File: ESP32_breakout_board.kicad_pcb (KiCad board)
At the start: 2 copper layers, 55.2 x 55.9 mm, 12 parts, among them J1 Conn_01x15, J2 Conn_01x15

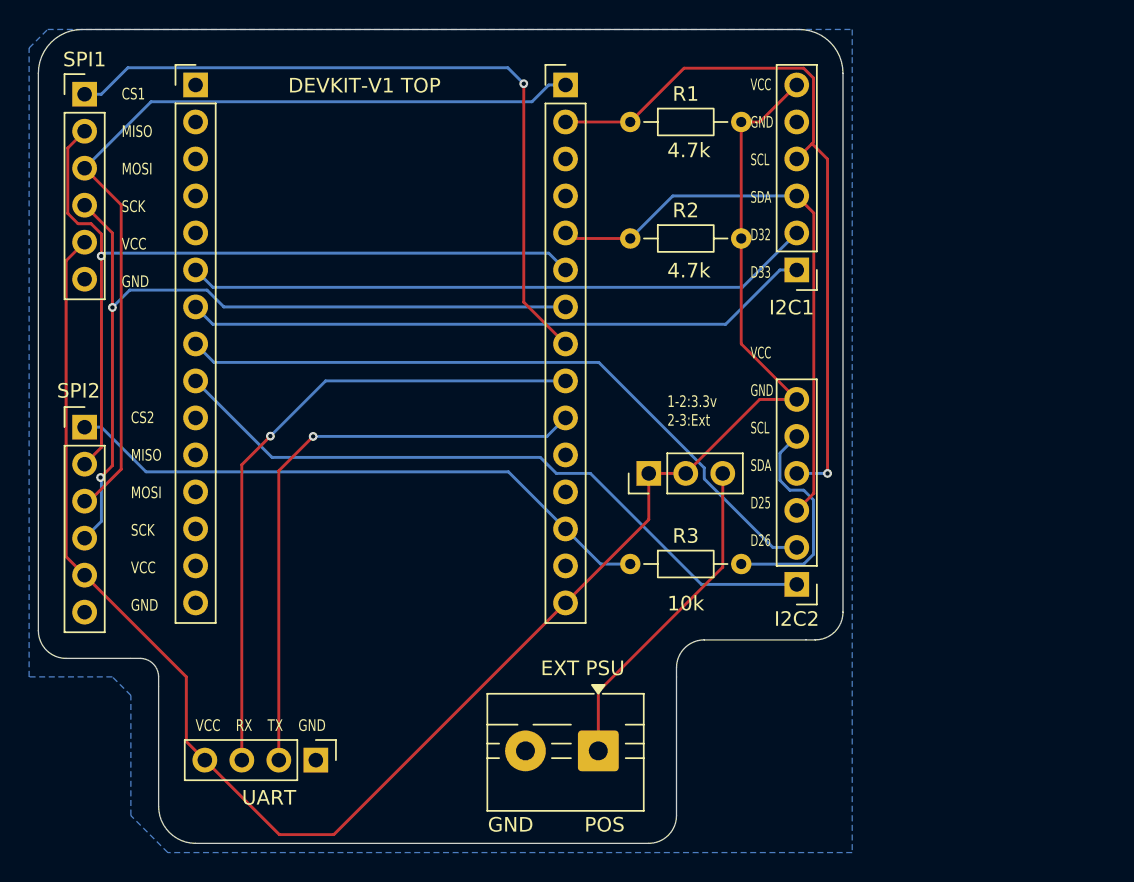
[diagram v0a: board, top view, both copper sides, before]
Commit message: changed design
removed the 10k pull down after careful consideration and cleaned up the design a bit
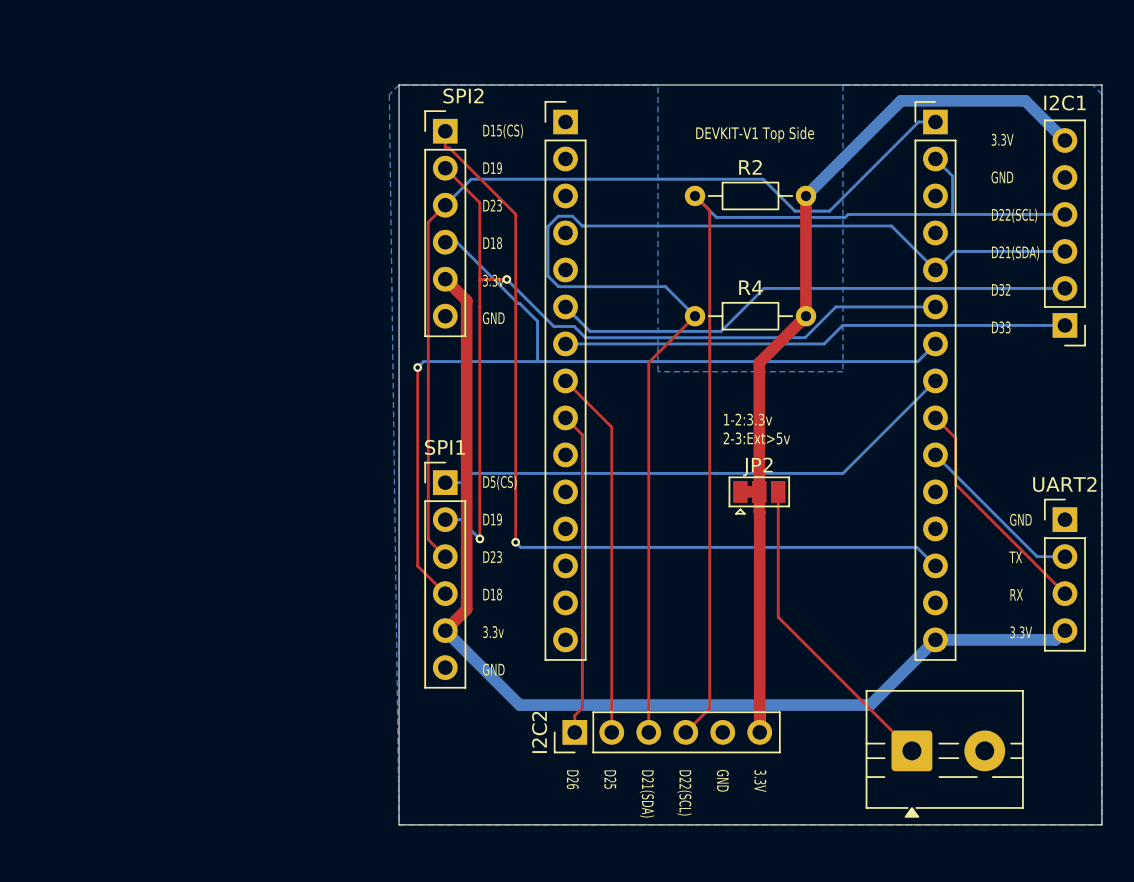
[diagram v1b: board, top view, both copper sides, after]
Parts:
- removed JP1: Power select jumper, Connector_PinHeader_2.54mm:PinHeader_1x03_P2.54mm_Vertical
- removed R1: 4.7k, Resistor_THT:R_Axial_DIN0204_L3.6mm_D1.6mm_P7.62mm_Horizontal
- removed R3: 10k, Resistor_THT:R_Axial_DIN0204_L3.6mm_D1.6mm_P7.62mm_Horizontal
- added JP2: SolderJumper_3_Open, Jumper:SolderJumper-3_P1.3mm_Open_Pad1.0x1.5mm, F.Cu at (140.3, 88.9)
- added R4: 4.7k, Resistor_THT:R_Axial_DIN0204_L3.6mm_D1.6mm_P7.62mm_Horizontal, F.Cu at (135.9, 76.8)
- moved UART2 54.0 mm to (161.3, 90.8), turned to 0 degrees
- moved SPI1 36.4 mm to (118.7, 88.3)
- moved SPI2 32.0 mm to (118.7, 64.1)
- moved J1 25.5 mm to (127.0, 63.5)
- moved J2 25.5 mm to (152.4, 63.5)
- moved Psu_power1 21.5 mm to (150.8, 106.7), turned to 0 degrees
- moved I2C1 18.8 mm to (161.3, 77.5)
- moved I2C2 18.3 mm to (127.6, 105.4), turned to 90 degrees
- moved R2 5.32 mm to (135.9, 68.6)
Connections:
- R2 pad 1: /D21 -> /D22
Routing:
- net /D21: track 39.8 -> 82.4 mm
- net /RX2: track 41.1 -> 11.8 mm, vias 1 -> 0
- net /TX2: track 44.9 -> 15.7 mm, vias 1 -> 0
- net /D26: track 47.1 -> 22.3 mm
- net /D25: track 47.5 -> 25.4 mm
- net /D15: track 41.4 -> 59.9 mm, vias 0 -> 1
- net /D22: track 50.1 -> 68.3 mm, vias 1 -> 0
- net GND: track 15.3 -> 0.00 mm
- net /D5: track 50.4 -> 36.5 mm, vias 1 -> 0
- net +3.3V: track 122.5 -> 135.1 mm
- net /D33: track 43.3 -> 34.8 mm
- net /D18: track 56.6 -> 63.9 mm, vias 2 -> 1
- net /D32: track 43.3 -> 36.2 mm
- net /D19: track 57.8 -> 63.2 mm, vias 1 -> 2
- net /D23: track 60.5 -> 62.9 mm
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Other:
- board size 55.2 x 55.9 mm -> 48.3 x 50.8 mm
- board text added: "1-2:3.3v 2-3:Ext>5v"
- board text added: "3.3V GND D22(SCL) D21(SDA) D25 D26"
- board text added: "3.3V GND D22(SCL) D21(SDA) D32 D33"
- board text added: "D15(CS) D19 D23 D18 3.3v GND"
- board text added: "D5(CS) D19 D23 D18 3.3v GND"
- board text added: "DEVKIT-V1 Top Side"
- board text added: "GND TX RX 3.3V"
- board text removed: "1-2:3.3v 2-3:Ext"
- board text removed: "10k"
- board text removed: "4.7k"
- board text removed: "CS1 MISO MOSI SCK VCC GND"
- board text removed: "CS2 MISO MOSI SCK VCC GND"
- board text removed: "DEVKIT-V1 TOP"
- board text removed: "EXT PSU"
- board text removed: "GND POS"
- board text removed: "I2C1"
- board text removed: "SPI2"
- board text removed: "UART"
- board text removed: "VCC GND SCL SDA D25 D26"
- board text removed: "VCC GND SCL SDA D32 D33"
- board text removed: "VCC RX TX GND"
